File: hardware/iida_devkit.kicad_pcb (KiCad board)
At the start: 4 copper layers, 180 x 64 mm, 160 parts, among them J1 B2B-PH-K-S, J10 PRPC001DAAN-RC, J11 PRPC006SAAN-RC, J12 PRPC004SAAN-RC, J13 PRPC001DAAN-RC, J14 PRPC006SAAN-RC, J15 G85D1160022HHR, J2 USB4110-GF-A, J3 PRPC001DAAN-RC, J4 PRPC001DAAN-RC, J5 PRPC001DAAN-RC, J6 PRPC001DAAN-RC, J7 PRPC001DAAN-RC, J8 SBH11-NBPC-D05-SM-BK, J9 PRPC006SAAN-RC, Q1 IRLML2246TRPBF, Q2 DMN2046U-7, Q3 DMN2046U-7, Q4 IRLML2246TRPBF, Q5 IRLML2246TRPBF, Q6 MMBT3904, U1 USBLC6-2SC6, U10 SARA-R500S-61B, U2 S-8240ADQ-M6T1U, U3 MCP73811T-420I-OT, U4 TPS62A01PDDCR, U5 AT25SF081B-SSHD-B, U6 MCP9808, U7 STM32L552CETx, U8 74AVC1T45DW-7, U9 74AVC1T45DW-7, Y1 ABS05-32.768KHZ-9-T, Y2 ECS-160-9-37-CKM-TR3

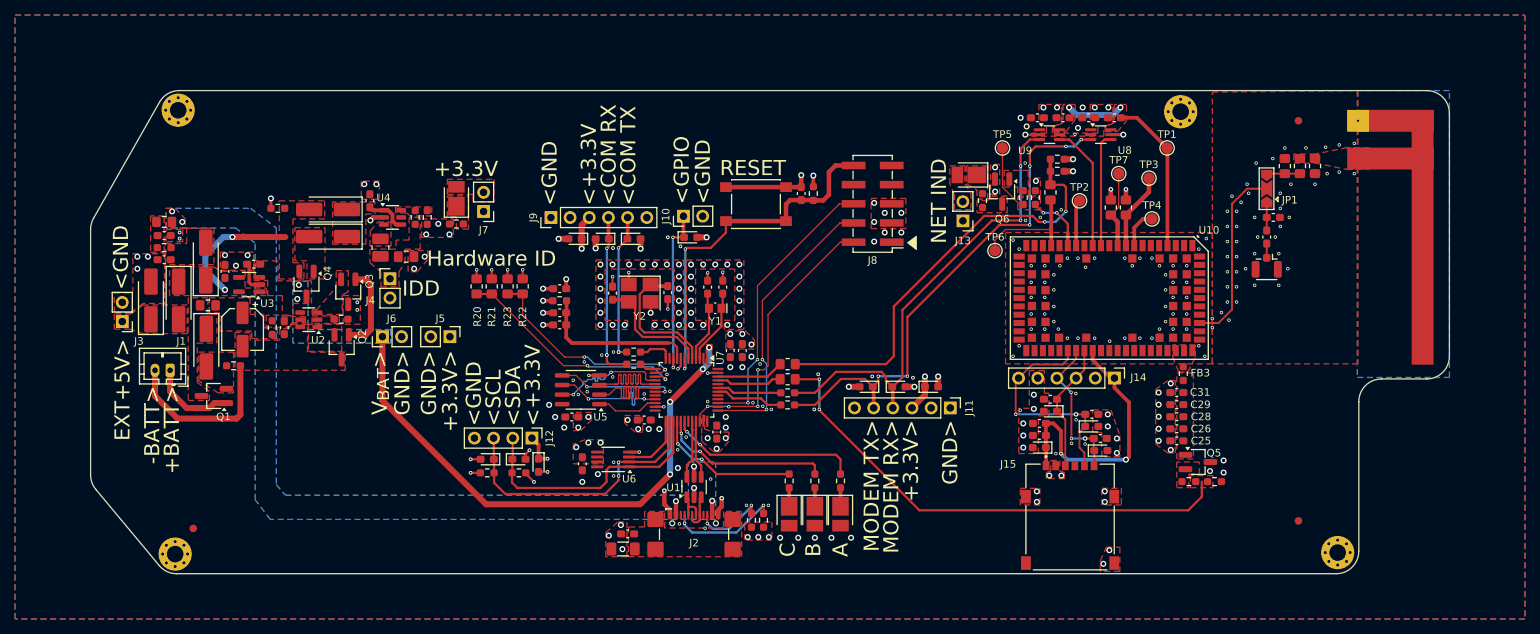
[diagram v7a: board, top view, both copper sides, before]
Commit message: HW: Fix programming header and layout
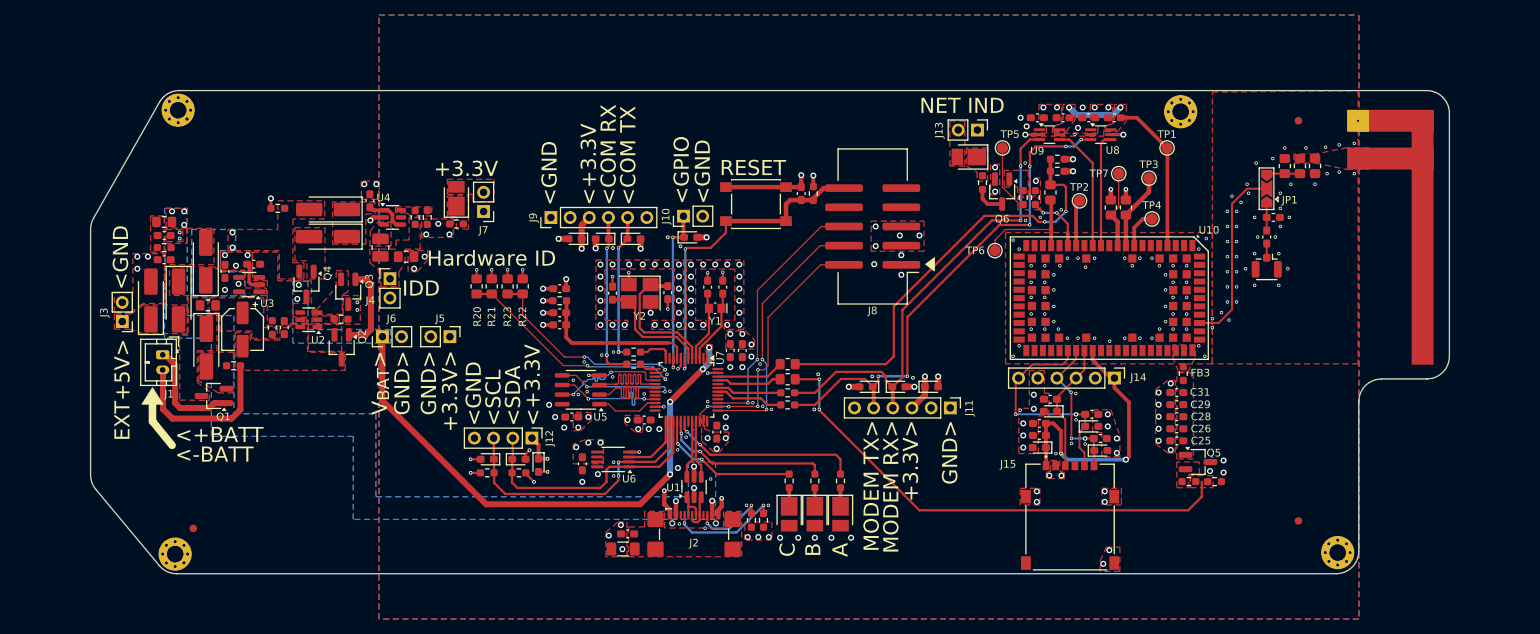
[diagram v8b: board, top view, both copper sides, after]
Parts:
- J8: footprint Connector_PinHeader_2.54mm:PinHeader_2x05_P2.54mm_Vertical_SMD -> Connector_IDC:IDC-Header_2x05_P2.54mm_Vertical_SMD
- moved J13 12.2 mm to (187.5, 75.2), turned to -90 degrees
- moved J8 3.00 mm to (173.6, 88.0)
- moved LED5 2.38 mm to (186.3, 78.8)
- moved R31 2.38 mm to (188.2, 82.2)
- moved J1 2.27 mm to (79.5, 105.0), turned to -90 degrees
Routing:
- net Net-(D2-K): track 17.3 -> 0.00 mm, vias 2 -> 4
- net /MCU/~{RESET}: track 48.1 -> 44.0 mm
- net Net-(Q6-C): track 0.00 -> 4.12 mm
- net Net-(J1-Pin_1): track 11.4 -> 14.6 mm
- net /MCU/SWO: track 37.2 -> 34.4 mm
- net /MCU/SWDIO: track 37.6 -> 34.8 mm
- net /MCU/SWCLK: track 37.5 -> 34.7 mm
- net Net-(D4-A): track 0.90 -> 0.00 mm
- net Net-(U1-VBUS): vias 5 -> 6
- added copper zone on B.Cu, net Net-(D2-K)
- removed copper zone on B.Cu, net GND
- removed copper zone on F.Cu, net Net-(Q6-C)
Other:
- board text added: "<+BATT"
- board text added: "<-BATT"
- board text removed: "+BATT>"
- board text removed: "-BATT>"
